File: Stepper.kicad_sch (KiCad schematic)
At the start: 64 parts, among them J1 Conn_02x18_Counter_Clockwise, SW1 STEP, SW2 RESET, SW3 MANUAL/~{AUTO}, X1 Power, X2 Address, X3 Data, X4 Mode, X5 Control, X6 Clock

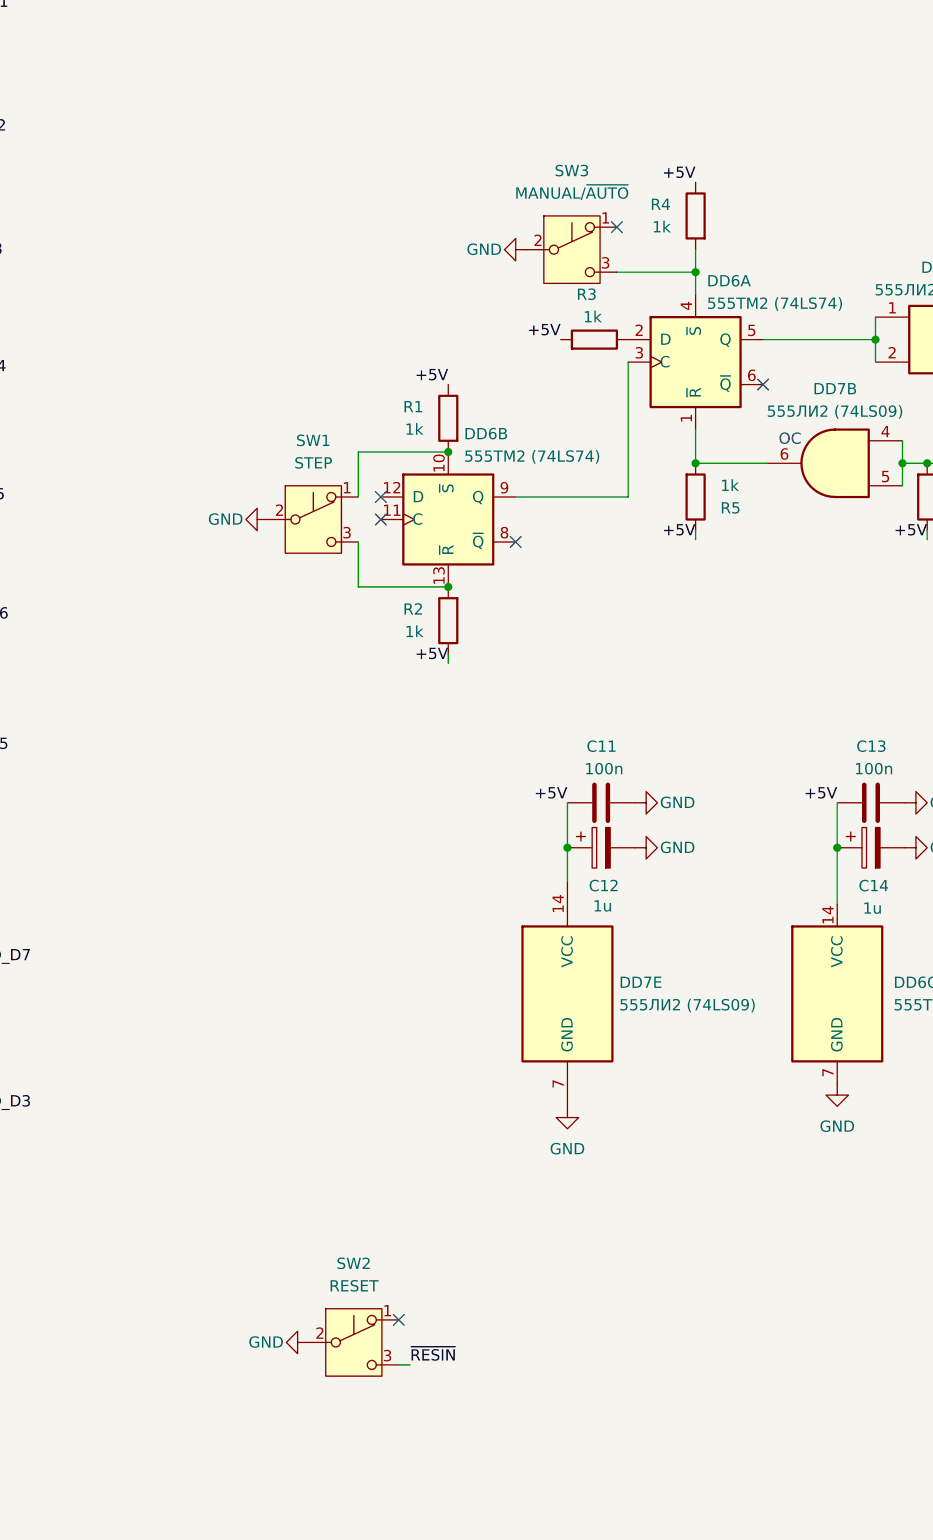
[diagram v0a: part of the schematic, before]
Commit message: Add files via upload
Fix button error and missed ground.
Исправлена ошибка кнопок и отсутствующих земель.
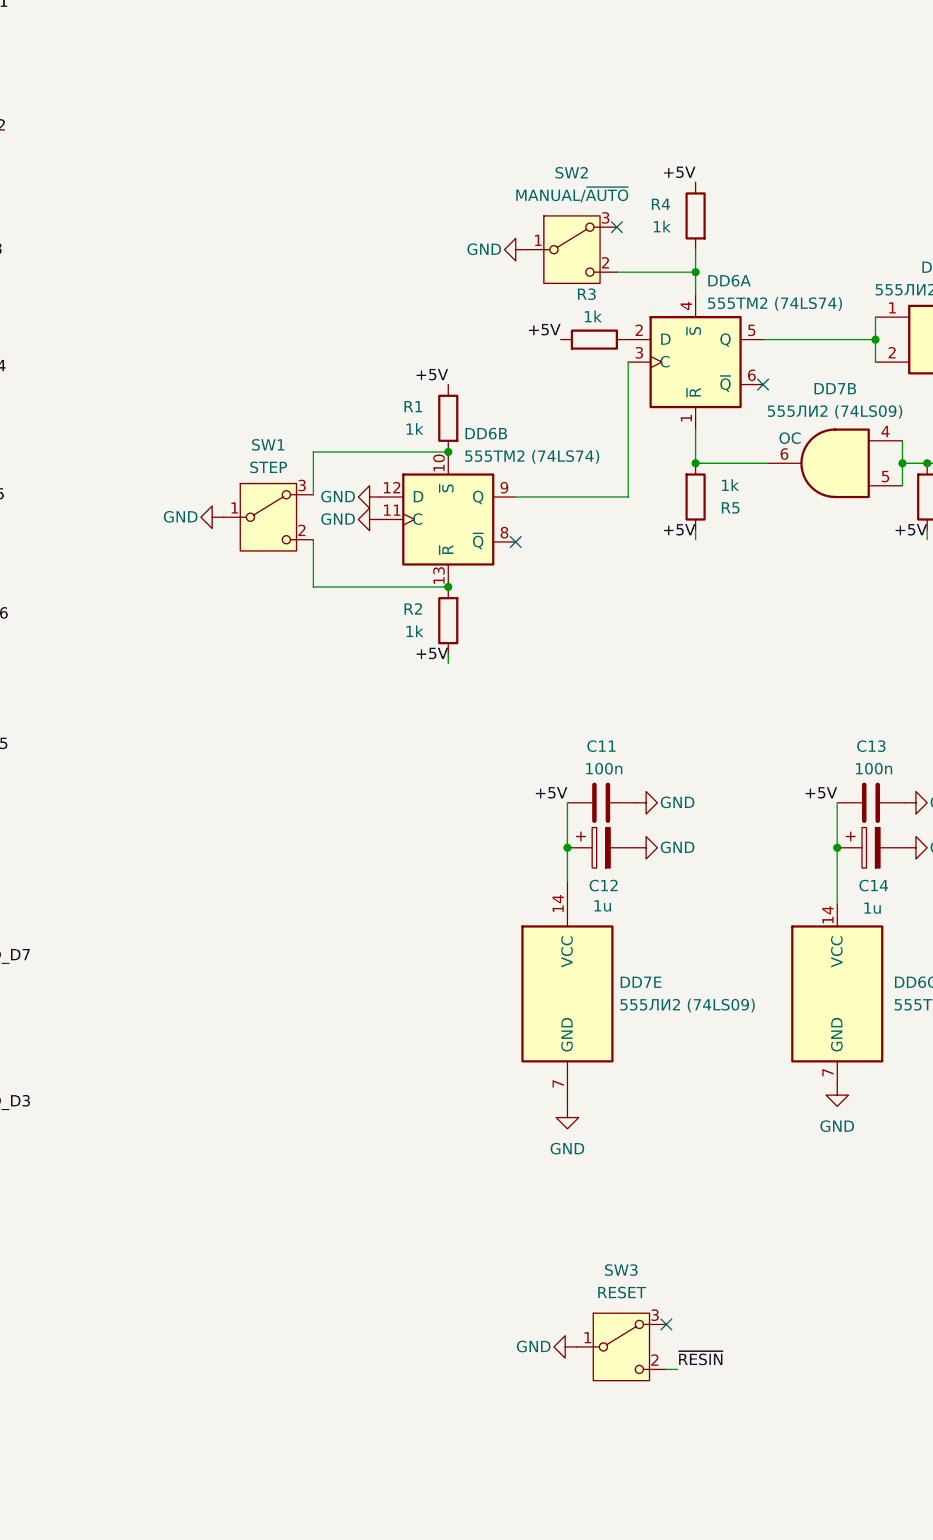
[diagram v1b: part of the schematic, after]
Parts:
- removed SW1: STEP, Button_Switch_THT:SW_Push_2P2T_Toggle_CK_PVA2OAH5xxxxxxV2, symbol Switch:SW_Push_SPDT
- removed SW2: RESET, Button_Switch_THT:SW_Push_2P2T_Toggle_CK_PVA2OAH5xxxxxxV2, symbol Switch:SW_Push_SPDT
- removed SW3: MANUAL/~{AUTO}, Button_Switch_THT:SW_Push_2P2T_Toggle_CK_PVA2OAH5xxxxxxV2, symbol Switch:SW_Push_SPDT
- added SW1: STEP, Button_Switch_THT:SW_Push_2P2T_Toggle_CK_PVA2OAH5xxxxxxV2, symbol Switch:SW_Wuerth_450301014042
- added SW2: MANUAL/~{AUTO}, Button_Switch_THT:SW_Push_2P2T_Toggle_CK_PVA2OAH5xxxxxxV2, symbol Switch:SW_Wuerth_450301014042
- added SW3: RESET, Button_Switch_THT:SW_Push_2P2T_Toggle_CK_PVA2OAH5xxxxxxV2, symbol Switch:SW_Wuerth_450301014042
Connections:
- net GND: now also DD6.11 (C), DD6.12 (D), SW1.1 (B), SW2.1 (B), SW3.1 (B)
- net ~{RESIN}: now also SW3.2 (C)
- net at DD6.4 (~{S}), R4.2: now also SW2.2 (C)
- net at DD6.13 (~{R}), R2.2: now also SW1.2 (C)
- net at DD6.10 (~{S}), R1.2: now also SW1.3 (A)
- no-connect marks 8 -> 6

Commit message: Add files via upload
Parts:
- C2: renamed from C9; value 100n -> 1u; footprint Capacitor_SMD:C_0805_2012Metric_Pad1.18x1.45mm_HandSolder -> Capacitor_Tantalum_SMD:CP_EIA-3216-18_Kemet-A_Pad1.58x1.35mm_HandSolder
- C5: renamed from C10; value 1u -> 100n; footprint Capacitor_Tantalum_SMD:CP_EIA-3216-18_Kemet-A_Pad1.58x1.35mm_HandSolder -> Capacitor_SMD:C_0805_2012Metric_Pad1.18x1.45mm_HandSolder
- C6: renamed from C3; value 100n -> 1u; footprint Capacitor_SMD:C_0805_2012Metric_Pad1.18x1.45mm_HandSolder -> Capacitor_Tantalum_SMD:CP_EIA-3216-18_Kemet-A_Pad1.58x1.35mm_HandSolder
- C7: renamed from C2; value 1u -> 100n; footprint Capacitor_Tantalum_SMD:CP_EIA-3216-18_Kemet-A_Pad1.58x1.35mm_HandSolder -> Capacitor_SMD:C_0805_2012Metric_Pad1.18x1.45mm_HandSolder
- DD6: renamed from DD7; value 555ЛИ2 (74LS09) -> 555ТМ2 (74LS74)
- DD7: renamed from DD6; value 555ТМ2 (74LS74) -> 555ЛИ2 (74LS09)
- SW1: renamed from SW3; value RESET -> STEP
- SW2: renamed from SW1; value STEP -> MANUAL/~{AUTO}
- SW3: renamed from SW2; value MANUAL/~{AUTO} -> RESET
- X1: renamed from X3; value Data -> Power; footprint Connector_PinHeader_2.54mm:PinHeader_1x08_P2.54mm_Vertical -> Connector_PinHeader_2.54mm:PinHeader_1x06_P2.54mm_Vertical
- X2: renamed from X5; value Control -> Address; footprint Connector_PinHeader_2.54mm:PinHeader_1x10_P2.54mm_Vertical -> Connector_PinHeader_2.54mm:PinHeader_1x16_P2.54mm_Vertical
- X3: renamed from X4; value Mode -> Data; footprint Connector_PinHeader_2.54mm:PinHeader_1x04_P2.54mm_Vertical -> Connector_PinHeader_2.54mm:PinHeader_1x08_P2.54mm_Vertical
- X4: renamed from X2; value Address -> Mode; footprint Connector_PinHeader_2.54mm:PinHeader_1x16_P2.54mm_Vertical -> Connector_PinHeader_2.54mm:PinHeader_1x04_P2.54mm_Vertical
- X5: renamed from X1; value Power -> Control; footprint Connector_PinHeader_2.54mm:PinHeader_1x06_P2.54mm_Vertical -> Connector_PinHeader_2.54mm:PinHeader_1x10_P2.54mm_Vertical
- renumbered C6 to C10, C13 to C11, C14 to C12, C11 to C13, C12 to C14, C7 to C3, C8 to C4, C4 to C8, C5 to C9, D5 to D1, D24 to D10, D21 to D11, D8 to D12, D12 to D13, D11 to D14, D20 to D15, D13 to D18, D18 to D19, D14 to D20, D19 to D21, D15 to D22, D10 to D23, D9 to D24, D4 to D3, D6 to D4, D1 to D5, D7 to D6, D3 to D7, D22 to D8, D23 to D9, DD4 to DD1, DD3 to DD1, DD1 to DD2, DD3 to DD2, DD5 to DD2, DD2 to DD3, DD4 to DD3, DD5 to DD3, DD5 to DD4, DD1 to DD4, DD3 to DD4, DD2 to DD5, DD1 to DD5, DD3 to DD5, R5 to R1, R4 to R2, R2 to R3, R1 to R4, R6 to R5, R3 to R6, RN3 to RN1, RN1 to RN2, RN2 to RN3
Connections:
- net INTE renamed ~{WRQ}
- net Single_BCLK renamed F2TTL
- net Single_OSC_TTL renamed OSC_TTL
